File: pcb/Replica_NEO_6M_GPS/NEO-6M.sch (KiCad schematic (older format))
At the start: 9 parts, among them J1 Conn_Coaxial, U2 NEO-6M-GPS

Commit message: se hicieron correcciones
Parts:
- U2: footprint XCVR_NEO-6M-GPS -> NEO-6M-GPS d:XCVR_NEO-6M-GPS
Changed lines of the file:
@@
 Title "Modulo GPS NEO 6M uBLOX"
 Date "2021-07-12"
-Rev ""
+Rev "1.0"
 Comp "Christian Canaan Castro Botek UBA - Argentina"
 Comment1 ""
@@
 F 0 "U2" H 5550 4367 50  0000 C CNN
 F 1 "NEO-6M-GPS" H 5550 4276 50  0000 C CNN
-F 2 "XCVR_NEO-6M-GPS" H 5550 3200 50  0001 L BNN
+F 2 "NEO-6M-GPS d:XCVR_NEO-6M-GPS" H 5550 3200 50  0001 L BNN
 F 3 "" H 5550 3200 50  0001 L BNN
 F 4 "R15" H 5550 3200 50  0001 L BNN "PARTREV"

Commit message: Se agregaron footprints y se hicieron correcciones menores
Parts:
- removed J1: Conn_Coaxial, symbol Connector:Conn_Coaxial
- added J1: CONUFL001-SMD-T, CONUFL001-SMD-T:LINX_CONUFL001-SMD-T, symbol CONUFL001-SMD-T:CONUFL001-SMD-T
- D2: footprint (none) -> LED_SMD:LED_0201_0603Metric_Pad0.64x0.40mm_HandSolder
- L1: footprint Inductor_SMD:L_0402_1005Metric_Pad0.77x0.64mm_HandSolder -> Inductor_SMD:L_0805_2012Metric_Pad1.15x1.40mm_HandSolder
- R2: value 22R -> 22K; footprint (none) -> Resistor_SMD:R_0805_2012Metric_Pad1.20x1.40mm_HandSolder
- R3, R4: footprint (none) -> Resistor_SMD:R_0805_2012Metric_Pad1.20x1.40mm_HandSolder
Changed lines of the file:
@@
 F 0 "R4" V 7393 3300 50  0000 C CNN
 F 1 "1K" V 7484 3300 50  0000 C CNN
-F 2 "" V 7530 3300 50  0001 C CNN
+F 2 "Resistor_SMD:R_0805_2012Metric_Pad1.20x1.40mm_HandSolder" V 7530 3300 50  0001 C CNN
 F 3 "~" H 7600 3300 50  0001 C CNN
 	1    7600 3300
@@
 F 0 "R3" V 4143 2450 50  0000 C CNN
 F 1 "1K" V 4234 2450 50  0000 C CNN
-F 2 "" V 4280 2450 50  0001 C CNN
+F 2 "Resistor_SMD:R_0805_2012Metric_Pad1.20x1.40mm_HandSolder" V 4280 2450 50  0001 C CNN
 F 3 "~" H 4350 2450 50  0001 C CNN
 	1    4350 2450
@@
 P 4100 3150
 F 0 "R2" V 3893 3150 50  0000 C CNN
-F 1 "22R" V 3984 3150 50  0000 C CNN
-F 2 "" V 4030 3150 50  0001 C CNN
+F 1 "22K" V 3984 3150 50  0000 C CNN
+F 2 "Resistor_SMD:R_0805_2012Metric_Pad1.20x1.40mm_HandSolder" V 4030 3150 50  0001 C CNN
 F 3 "~" H 4100 3150 50  0001 C CNN
 	1    4100 3150
@@
 F 0 "D2" H 3893 2667 50  0000 C CNN
 F 1 "FIX" H 3893 2576 50  0000 C CNN
-F 2 "" H 3900 2450 50  0001 C CNN
+F 2 "LED_SMD:LED_0201_0603Metric_Pad0.64x0.40mm_HandSolder" H 3900 2450 50  0001 C CNN
 F 3 "~" H 3900 2450 50  0001 C CNN
 	1    3900 2450
@@
 F 0 "L1" V 3840 3150 50  0000 C CNN
 F 1 "27uH" V 3749 3150 50  0000 C CNN
-F 2 "Inductor_SMD:L_0402_1005Metric_Pad0.77x0.64mm_HandSolder" H 3650 3150 50  0001 C CNN
+F 2 "Inductor_SMD:L_0805_2012Metric_Pad1.15x1.40mm_HandSolder" H 3650 3150 50  0001 C CNN
 F 3 "~" H 3650 3150 50  0001 C CNN
 	1    3650 3150
@@
 Wire Wire Line
 	3350 3150 3500 3150
-Wire Wire Line
-	3350 3150 3150 3150
 Connection ~ 3350 3150
 $Comp
@@
 	1    0    0    -1
 $EndComp
-Wire Wire Line
-	2950 3350 2950 3500
 $Comp
 L Device:Battery_Cell BT1
@@
 Text Label 6500 3100 2    50   ~ 0
 TXD1
-Text Notes 2800 3200 2    50   ~ 0
+Text Notes 2650 3150 2    50   ~ 0
 Antenna
-$Comp
-L Connector:Conn_Coaxial J1
-U 1 1 60F4FF8E
-P 2950 3150
-F 0 "J1" V 3129 3125 50  0000 L TNN
-F 1 "Conn_Coaxial" V 3089 3034 50  0000 L CNN
-F 2 "" H 2950 3150 50  0001 C CNN
-F 3 " ~" H 2950 3150 50  0001 C CNN
-	1    2950 3150
-	0    -1   -1   0
-$EndComp
 Wire Wire Line
 	6350 2900 6500 2900
@@
 Text HLabel 6500 3000 2    50   BiDi ~ 0
 SCL2
+$Comp
+L CONUFL001-SMD-T:CONUFL001-SMD-T J1
+U 1 1 6108E865
+P 2850 3250
+F 0 "J1" H 2844 3557 50  0000 C CNN
+F 1 "CONUFL001-SMD-T" H 2844 3466 50  0000 C CNN
+F 2 "CONUFL001-SMD-T:LINX_CONUFL001-SMD-T" H 2850 3250 50  0001 L BNN
+F 3 "" H 2850 3250 50  0001 L BNN
+F 4 "B" H 2850 3250 50  0001 L BNN "PARTREV"
+F 5 "Linx Technologies" H 2850 3250 50  0001 L BNN "MANUFACTURER"
+F 6 "Manufacturer Recommendations" H 2850 3250 50  0001 L BNN "STANDARD"
+	1    2850 3250
+	1    0    0    -1
+$EndComp
+Wire Wire Line
+	2950 3150 3350 3150
+Wire Wire Line
+	2950 3250 2950 3500
 $EndSCHEMATC

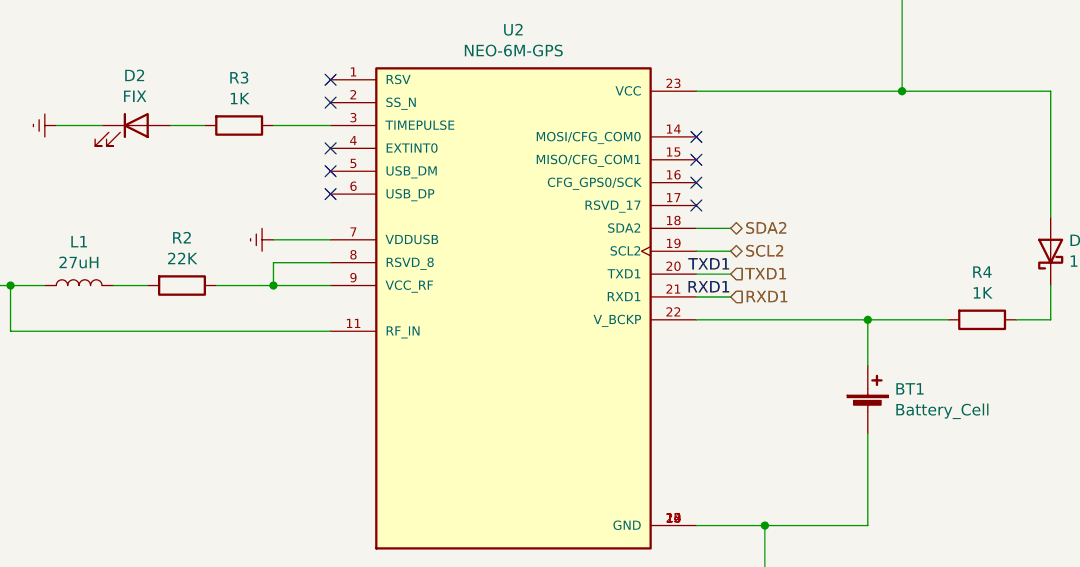
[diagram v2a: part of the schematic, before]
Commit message: Se hicieron correcciones y se avanzo con el PCB
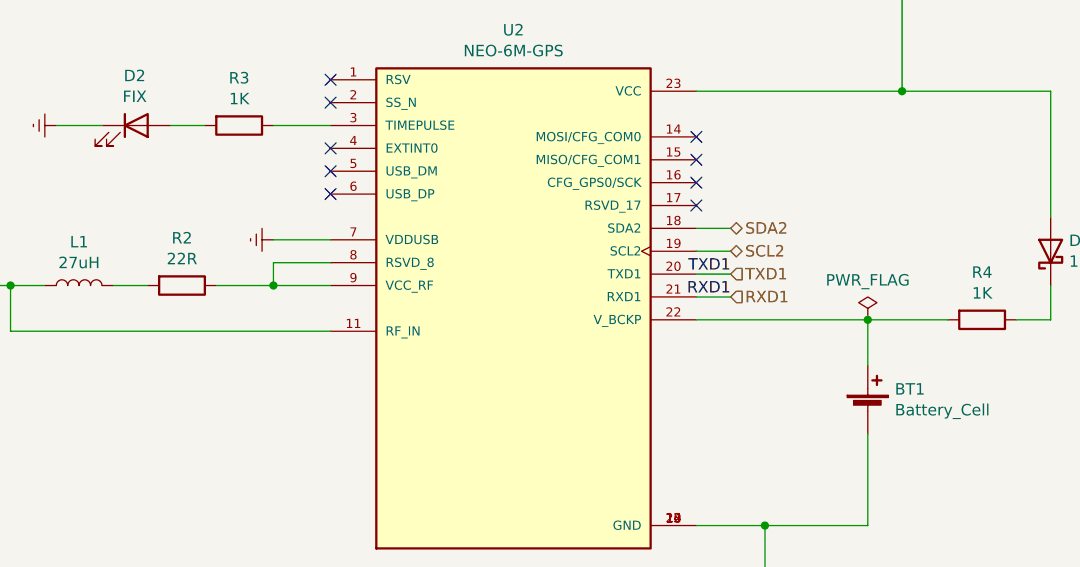
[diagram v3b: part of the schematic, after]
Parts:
- D3: footprint Diode_THT:D_DO-41_SOD81_P10.16mm_Horizontal -> Diode_SMD:D_0805_2012Metric_Pad1.15x1.40mm_HandSolder
- R2: value 22K -> 22R
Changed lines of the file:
@@
 P 4100 3150
 F 0 "R2" V 3893 3150 50  0000 C CNN
-F 1 "22K" V 3984 3150 50  0000 C CNN
+F 1 "22R" V 3984 3150 50  0000 C CNN
 F 2 "Resistor_SMD:R_0805_2012Metric_Pad1.20x1.40mm_HandSolder" V 4030 3150 50  0001 C CNN
 F 3 "~" H 4100 3150 50  0001 C CNN
@@
 F 0 "D3" V 7946 2920 50  0000 R CNN
 F 1 "1N5817" V 7855 2920 50  0000 R CNN
-F 2 "Diode_THT:D_DO-41_SOD81_P10.16mm_Horizontal" H 7900 2825 50  0001 C CNN
+F 2 "Diode_SMD:D_0805_2012Metric_Pad1.15x1.40mm_HandSolder" H 7900 2825 50  0001 C CNN
 F 3 "http://www.vishay.com/docs/88525/1n5817.pdf" H 7900 3000 50  0001 C CNN
 	1    7900 3000
@@
 Connection ~ 3350 3150
 $Comp
-L power:Earth #PWR010
-U 1 1 60F55298
-P 2950 3500
-F 0 "#PWR010" H 2950 3250 50  0001 C CNN
-F 1 "Earth" H 2950 3350 50  0001 C CNN
-F 2 "" H 2950 3500 50  0001 C CNN
-F 3 "~" H 2950 3500 50  0001 C CNN
-	1    2950 3500
-	1    0    0    -1
-$EndComp
-$Comp
 L Device:Battery_Cell BT1
 U 1 1 60F63945
@@
 Wire Wire Line
 	6350 3200 6500 3200
-Wire Wire Line
-	6650 4450 6650 4200
 Connection ~ 6650 4200
 Wire Wire Line
@@
 Wire Wire Line
 	6350 2300 7250 2300
-Wire Wire Line
-	7250 1900 7250 2300
 Connection ~ 7250 2300
 Wire Wire Line
@@
 Wire Wire Line
 	2950 3150 3350 3150
+$Comp
+L power:PWR_FLAG #FLG0101
+U 1 1 610A5A1B
+P 7100 3300
+F 0 "#FLG0101" H 7100 3375 50  0001 C CNN
+F 1 "PWR_FLAG" H 7100 3473 50  0000 C CNN
+F 2 "" H 7100 3300 50  0001 C CNN
+F 3 "~" H 7100 3300 50  0001 C CNN
+	1    7100 3300
+	1    0    0    -1
+$EndComp
+Wire Wire Line
+	7250 1900 7250 2300
+$Comp
+L power:Earth #PWR010
+U 1 1 60F55298
+P 2950 3500
+F 0 "#PWR010" H 2950 3250 50  0001 C CNN
+F 1 "Earth" H 2950 3350 50  0001 C CNN
+F 2 "" H 2950 3500 50  0001 C CNN
+F 3 "~" H 2950 3500 50  0001 C CNN
+	1    2950 3500
+	1    0    0    -1
+$EndComp
+Wire Wire Line
+	6650 4450 6650 4200
 Wire Wire Line
 	2950 3250 2950 3500

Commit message: Se hicieron cambiaron los footprints de los LEDS D1,D2
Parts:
- D2: footprint LED_SMD:LED_0201_0603Metric_Pad0.64x0.40mm_HandSolder -> LED_SMD:LED_0805_2012Metric_Pad1.15x1.40mm_HandSolder
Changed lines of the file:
@@
 F 0 "D2" H 3893 2667 50  0000 C CNN
 F 1 "FIX" H 3893 2576 50  0000 C CNN
-F 2 "LED_SMD:LED_0201_0603Metric_Pad0.64x0.40mm_HandSolder" H 3900 2450 50  0001 C CNN
+F 2 "LED_SMD:LED_0805_2012Metric_Pad1.15x1.40mm_HandSolder" H 3900 2450 50  0001 C CNN
 F 3 "~" H 3900 2450 50  0001 C CNN
 	1    3900 2450

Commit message: Se acomodaron archivos y se hicieron retoques
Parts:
- removed BT1: Battery_Cell, Battery:BatteryHolder_Keystone_2998_1x6.8mm, symbol Device:Battery_Cell
- added B1: MS621FE, MS621FE:MS621FE, symbol MS621FE:MS621FE
- J1: symbol CONUFL001-SMD-T:CONUFL001-SMD-T -> Replica_NEO_6M_GPS-rescue:CONUFL001-SMD-T-CONUFL001-SMD-T
- U2: symbol NEO-6M-GPS:NEO-6M-GPS -> Replica_NEO_6M_GPS-rescue:NEO-6M-GPS-NEO-6M-GPS
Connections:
- net GND: now also B1.-
- net at R4.2, U2.22 (V_BCKP): now also B1.+
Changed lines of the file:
@@
 $EndDescr
 $Comp
-L NEO-6M-GPS:NEO-6M-GPS U2
+L Replica_NEO_6M_GPS-rescue:NEO-6M-GPS-NEO-6M-GPS U2
 U 1 1 60ECA057
 P 5550 3200
@@
 	3350 3150 3500 3150
 Connection ~ 3350 3150
-$Comp
-L Device:Battery_Cell BT1
-U 1 1 60F63945
-P 7100 3700
-F 0 "BT1" H 7218 3796 50  0000 L CNN
-F 1 "Battery_Cell" H 7218 3705 50  0000 L CNN
-F 2 "Battery:BatteryHolder_Keystone_2998_1x6.8mm" V 7100 3760 50  0001 C CNN
-F 3 "~" V 7100 3760 50  0001 C CNN
-	1    7100 3700
-	1    0    0    -1
-$EndComp
 Wire Wire Line
 	6350 4200 6650 4200
-Wire Wire Line
-	7100 4200 7100 3800
 Wire Wire Line
 	7100 3500 7100 3300
@@
 SCL2
 $Comp
-L CONUFL001-SMD-T:CONUFL001-SMD-T J1
+L Replica_NEO_6M_GPS-rescue:CONUFL001-SMD-T-CONUFL001-SMD-T J1
 U 1 1 6108E865
 P 2850 3250
+AR Path="/6108E865" Ref="J1"  Part="1"
+AR Path="/60EC55A9/6108E865" Ref="J1"  Part="1"
 F 0 "J1" H 2844 3557 50  0000 C CNN
 F 1 "CONUFL001-SMD-T" H 2844 3466 50  0000 C CNN
@@
 Wire Wire Line
 	2950 3250 2950 3500
+$Comp
+L MS621FE:MS621FE B1
+U 1 1 611B4D84
+P 7100 3700
+F 0 "B1" V 7146 3567 50  0000 R CNN
+F 1 "MS621FE" V 7055 3567 50  0000 R CNN
+F 2 "MS621FE:MS621FE" H 7100 3700 50  0001 L BNN
+F 3 "" H 7100 3700 50  0001 L BNN
+	1    7100 3700
+	0    -1   -1   0
+$EndComp
+Wire Wire Line
+	7100 3900 7100 4200
 $EndSCHEMATC

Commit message: se retoco el esquematico
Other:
- moved on the sheet: B1, D2, D3, J1, L1, R2, R3, R4, U2
